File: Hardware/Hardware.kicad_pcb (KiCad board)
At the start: 2 copper layers, 15 parts, among them J1 Conn_01x02, J2 Conn_01x04, J3 Conn_01x03, J4 Conn_01x02, J5 Conn_01x06, J6 Conn_01x08, U1 ESP32-WROOM-32

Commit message: Routing was done
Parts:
- C1, C2, C3: footprint Connector_PinHeader_2.54mm:PinHeader_1x02_P2.54mm_Vertical -> Capacitor_THT:CP_Radial_D4.0mm_P2.00mm
- R1, R2, R3, R4, R5: footprint Connector_PinHeader_2.54mm:PinHeader_1x02_P2.54mm_Vertical -> Resistor_THT:R_Axial_DIN0204_L3.6mm_D1.6mm_P2.54mm_Vertical
- moved J2 85.6 mm to (85.1, 121.9), turned to 90 degrees
- moved J4 68.5 mm to (85.1, 88.9), turned to 180 degrees
- moved R3 62.8 mm to (93.5, 114.3)
- moved R2 59.1 mm to (93.5, 111.8)
- moved R1 49.9 mm to (139.7, 90.2), turned to 90 degrees
- moved R4 49.1 mm to (107.2, 121.4), turned to 90 degrees
- moved C1 33.0 mm to (136.1, 84.3), turned to 180 degrees
- moved R5 32.2 mm to (115.8, 121.4), turned to 90 degrees
- moved C3 27.3 mm to (136.1, 92.9), turned to 180 degrees
- moved C2 26.9 mm to (136.1, 101.6), turned to 180 degrees
- moved J3 26.2 mm to (134.6, 111.8)
- moved J1 12.4 mm to (134.6, 124.5)
- moved J6 11.4 mm to (85.1, 114.3)
- moved J5 4.26 mm to (115.6, 129.5)
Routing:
- net Net-(C1-Pad1): track 0.00 -> 50.2 mm, vias 0 -> 2
- net /IO23: track 0.00 -> 47.5 mm, vias 0 -> 2
- net GND: track 0.00 -> 37.1 mm, vias 0 -> 3
- net /SDI: track 0.00 -> 34.2 mm, vias 0 -> 2
- net Net-(J2-Pad4): track 0.00 -> 25.6 mm, vias 0 -> 3
- net /SDO: track 0.00 -> 24.2 mm, vias 0 -> 1
- net /IO35: track 0.00 -> 21.2 mm
- net /IO33: track 0.00 -> 20.5 mm
- net Net-(J2-Pad3): track 0.00 -> 20.4 mm
- net /RXD: track 0.00 -> 20.3 mm
- net /IO27: track 0.00 -> 19.6 mm
- net /IO25: track 0.00 -> 19.6 mm, vias 0 -> 2
- net /TXD: track 0.00 -> 19.2 mm
- net /Boot_Option: track 0.00 -> 19.2 mm
- net /IO34: track 0.00 -> 19.0 mm, vias 0 -> 2
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- added copper zone on B.Cu, net /VDD33
- added copper zone on B.Cu, net GND

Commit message: quality of life improvements
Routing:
- added copper zone on F.Cu, net /VDD33
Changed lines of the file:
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@@
+    )
+  )
+  (zone (net 3) (net_name /VDD33) (layer B.Cu) (hatch edge 0.508)
+    (connect_pads (clearance 0.508))
+    (min_thickness 0.254)
+    (fill yes (arc_segments 32) (thermal_gap 0.508) (thermal_bridge_width 0.508))
+    (polygon
+      (pts
+        (xy 77.47 78.74) (xy 68.58 80.01) (xy 72.39 68.58)
+      )
+    )
+  )
+  (zone (net 3) (net_name /VDD33) (layer F.Cu) (hatch edge 0.508)
+    (connect_pads (clearance 0.508))
+    (min_thickness 0.254)
+    (fill yes (arc_segments 32) (thermal_gap 0.508) (thermal_bridge_width 0.508))
+    (polygon
+      (pts
+        (xy 95.25 97.79) (xy 127 97.79) (xy 127 78.74) (xy 143.51 78.74) (xy 143.51 135.89)
+        (xy 77.47 135.89) (xy 77.47 78.74) (xy 95.25 78.74)
+      )
     )
   )

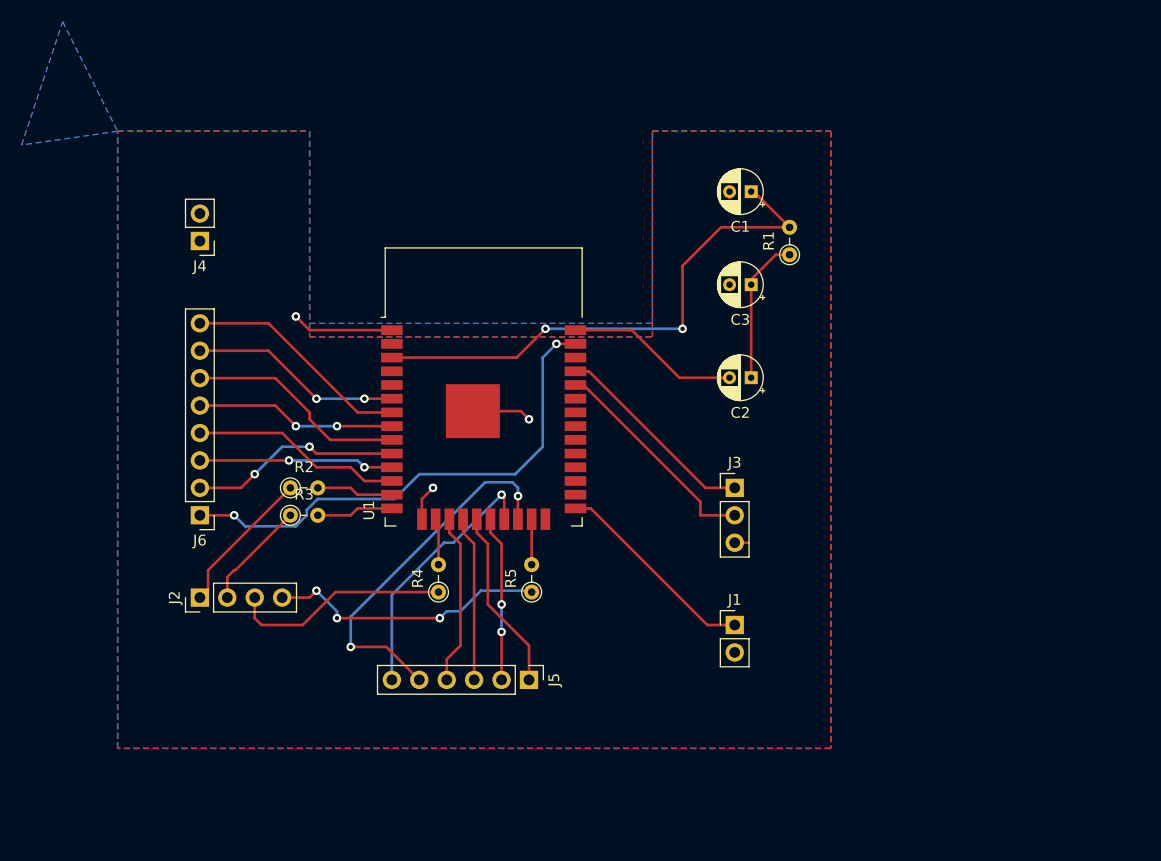
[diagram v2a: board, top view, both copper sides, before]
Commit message: Motor port addition and ground plane fix
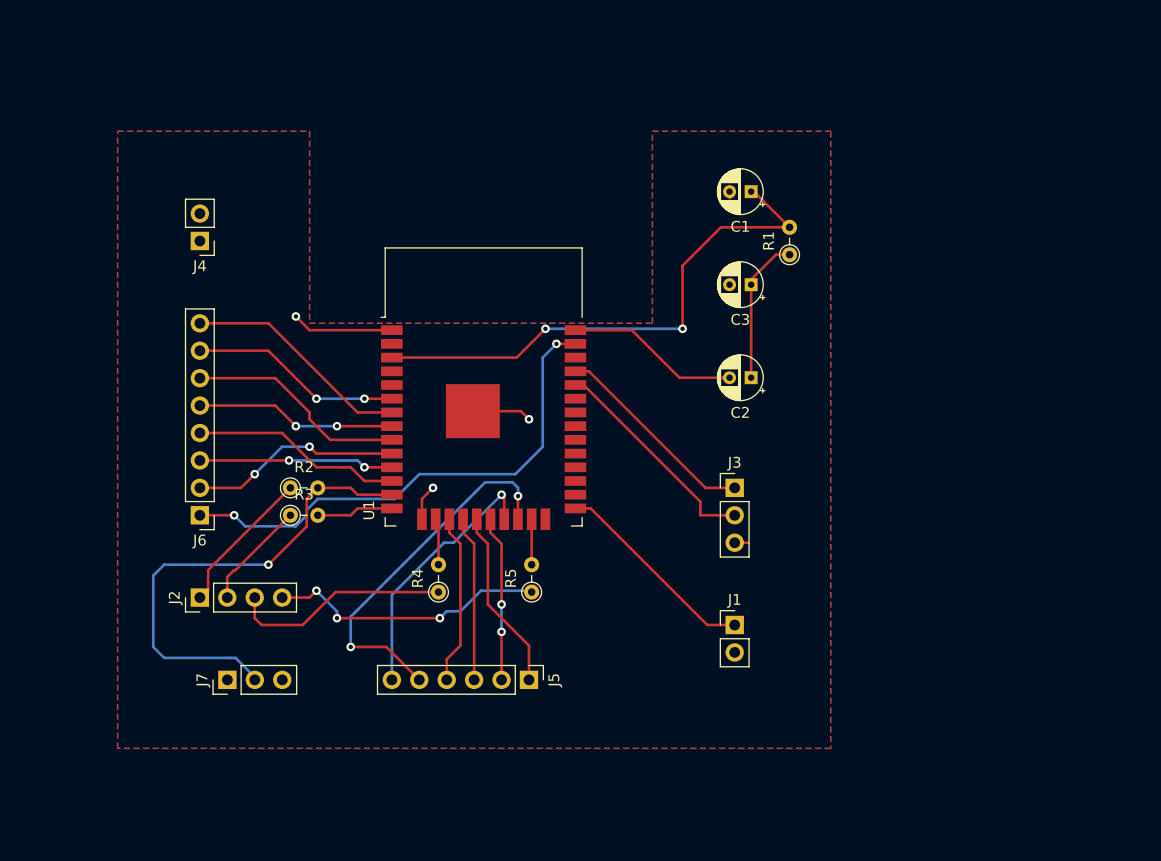
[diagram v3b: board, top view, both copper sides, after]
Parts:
- added J7: Conn_01x03, Connector_PinHeader_2.54mm:PinHeader_1x03_P2.54mm_Vertical, F.Cu at (87.6, 129.5)
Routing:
- net /MTMS: track 7.25 -> 44.9 mm, vias 0 -> 1
- removed copper zone on B.Cu, net /VDD33

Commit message: Silkscreen was added.
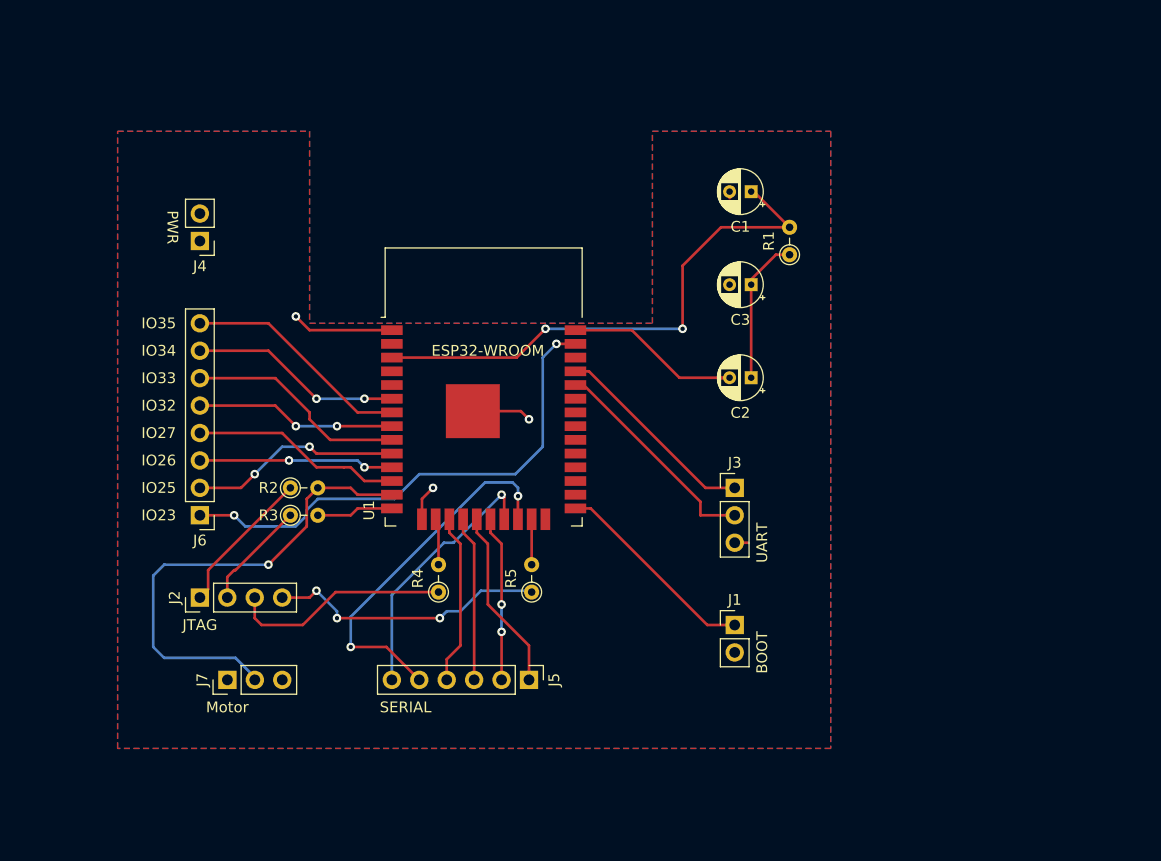
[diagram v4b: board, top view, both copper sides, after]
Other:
- board text added: "BOOT"
- board text added: "ESP32-WROOM"
- board text added: "IO23"
- board text added: "IO25"
- board text added: "IO26"
- board text added: "IO27"
- board text added: "IO32"
- board text added: "IO33"
- board text added: "IO34"
- board text added: "IO35"
- board text added: "JTAG"
- board text added: "Motor"
- board text added: "PWR"
- board text added: "SERIAL"
- board text added: "UART"
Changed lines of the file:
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@@
   (general
     (thickness 1.6)
-    (drawings 4)
+    (drawings 19)
     (tracks 180)
     (zones 0)
@@
   (page A4)
   (layers
-    (0 F.Cu signal)
-    (31 B.Cu signal)
+    (0 F.Cu signal hide)
+    (31 B.Cu signal hide)
     (32 B.Adhes user)
     (33 F.Adhes user)
@@
     (descr "Resistor, Axial_DIN0204 series, Axial, Vertical, pin pitch=2.54mm, 0.167W, length*diameter=3.6*1.6mm^2, http://cdn-reichelt.de/documents/datenblatt/B400/1_4W%23YAG.pdf")
     (tags "Resistor Axial_DIN0204 series Axial Vertical pin pitch 2.54mm 0.167W length 3.6mm diameter 1.6mm")
-    (fp_text reference R3 (at 1.27 -1.92) (layer F.SilkS)
+    (fp_text reference R3 (at -2.032 0) (layer F.SilkS)
       (effects (font (size 1 1) (thickness 0.15)))
     )
@@
     (descr "Resistor, Axial_DIN0204 series, Axial, Vertical, pin pitch=2.54mm, 0.167W, length*diameter=3.6*1.6mm^2, http://cdn-reichelt.de/documents/datenblatt/B400/1_4W%23YAG.pdf")
     (tags "Resistor Axial_DIN0204 series Axial Vertical pin pitch 2.54mm 0.167W length 3.6mm diameter 1.6mm")
-    (fp_text reference R2 (at 1.27 -1.92) (layer F.SilkS)
+    (fp_text reference R2 (at -2.032 0) (layer F.SilkS)
       (effects (font (size 1 1) (thickness 0.15)))
     )
@@
     )
   )
+  (gr_text SERIAL (at 104.14 132.08) (layer F.SilkS)
+    (effects (font (size 1 1) (thickness 0.15)))
+  )
+  (gr_text BOOT (at 137.16 127 90) (layer F.SilkS)
+    (effects (font (size 1 1) (thickness 0.15)))
+  )
+  (gr_text UART (at 137.16 116.84 90) (layer F.SilkS)
+    (effects (font (size 1 1) (thickness 0.15)))
+  )
+  (gr_text ESP32-WROOM (at 111.76 99.06) (layer F.SilkS)
+    (effects (font (size 1 1) (thickness 0.15)))
+  )
+  (gr_text PWR (at 82.55 87.63 270) (layer F.SilkS)
+    (effects (font (size 1 1) (thickness 0.15)))
+  )
+  (gr_text IO35 (at 81.28 96.52) (layer F.SilkS)
+    (effects (font (size 1 1) (thickness 0.15)))
+  )
+  (gr_text IO34 (at 81.28 99.06) (layer F.SilkS)
+    (effects (font (size 1 1) (thickness 0.15)))
+  )
+  (gr_text IO33 (at 81.28 101.6) (layer F.SilkS)
+    (effects (font (size 1 1) (thickness 0.15)))
+  )
+  (gr_text IO32 (at 81.28 104.14) (layer F.SilkS)
+    (effects (font (size 1 1) (thickness 0.15)))
+  )
+  (gr_text IO27 (at 81.28 106.68) (layer F.SilkS)
+    (effects (font (size 1 1) (thickness 0.15)))
+  )
+  (gr_text IO26 (at 81.28 109.22) (layer F.SilkS)
+    (effects (font (size 1 1) (thickness 0.15)))
+  )
+  (gr_text IO25 (at 81.28 111.76) (layer F.SilkS)
+    (effects (font (size 1 1) (thickness 0.15)))
+  )
+  (gr_text IO23 (at 81.28 114.3) (layer F.SilkS)
+    (effects (font (size 1 1) (thickness 0.15)))
+  )
+  (gr_text JTAG (at 85.09 124.46) (layer F.SilkS)
+    (effects (font (size 1 1) (thickness 0.15)))
+  )
+  (gr_text Motor (at 87.63 132.08) (layer F.SilkS)
+    (effects (font (size 1 1) (thickness 0.15)))
+  )
   (gr_line (start 143.51 78.74) (end 77.47 78.74) (layer Dwgs.User) (width 0.15))

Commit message: battery connector update
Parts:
- J4: footprint Connector_PinHeader_2.54mm:PinHeader_1x02_P2.54mm_Vertical -> Connector_PinHeader_1.00mm:PinHeader_1x02_P1.00mm_Vertical
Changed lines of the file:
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@@
     (add_net "Net-(U1-Pad5)")
+  )
+  (module Connector_PinHeader_1.00mm:PinHeader_1x02_P1.00mm_Vertical (layer F.Cu)
+    (at 85.09 88.9 180)
+    (descr "Through hole straight pin header, 1x02, 1.00mm pitch, single row")
+    (tags "Through hole pin header THT 1x02 1.00mm single row")
+    (fp_text reference J4 (at 0 -1.56) (layer F.SilkS)
+      (effects (font (size 1 1) (thickness 0.15)))
+    )
+    (fp_text value Conn_01x02 (at 0 2.56) (layer F.Fab)
+      (effects (font (size 1 1) (thickness 0.15)))
+    )
+    (fp_text user %R (at 0 0.5 90) (layer F.Fab)
+      (effects (font (size 0.76 0.76) (thickness 0.114)))
+    )
+    (fp_line (start -0.3175 -0.5) (end 0.635 -0.5) (layer F.Fab) (width 0.1))
+    (fp_line (start 0.635 -0.5) (end 0.635 1.5) (layer F.Fab) (width 0.1))
+    (fp_line (start 0.635 1.5) (end -0.635 1.5) (layer F.Fab) (width 0.1))
+    (fp_line (start -0.635 1.5) (end -0.635 -0.1825) (layer F.Fab) (width 0.1))
+    (fp_line (start -0.635 -0.1825) (end -0.3175 -0.5) (layer F.Fab) (width 0.1))
+    (fp_line (start -0.695 1.56) (end -0.394493 1.56) (layer F.SilkS) (width 0.12))
+    (fp_line (start 0.394493 1.56) (end 0.695 1.56) (layer F.SilkS) (width 0.12))
+    (fp_line (start -0.695 0.685) (end -0.695 1.56) (layer F.SilkS) (width 0.12))
+    (fp_line (start 0.695 0.685) (end 0.695 1.56) (layer F.SilkS) (width 0.12))
+    (fp_line (start -0.695 0.685) (end -0.608276 0.685) (layer F.SilkS) (width 0.12))
+    (fp_line (start 0.608276 0.685) (end 0.695 0.685) (layer F.SilkS) (width 0.12))
+    (fp_line (start -0.695 0) (end -0.695 -0.685) (layer F.SilkS) (width 0.12))
+    (fp_line (start -0.695 -0.685) (end 0 -0.685) (layer F.SilkS) (width 0.12))
+    (fp_line (start -1.15 -1) (end -1.15 2) (layer F.CrtYd) (width 0.05))
+    (fp_line (start -1.15 2) (end 1.15 2) (layer F.CrtYd) (width 0.05))
+    (fp_line (start 1.15 2) (end 1.15 -1) (layer F.CrtYd) (width 0.05))
+    (fp_line (start 1.15 -1) (end -1.15 -1) (layer F.CrtYd) (width 0.05))
+    (pad 2 thru_hole oval (at 0 1 180) (size 0.85 0.85) (drill 0.5) (layers *.Cu *.Mask)
+      (net 1 GND))
+    (pad 1 thru_hole rect (at 0 0 180) (size 0.85 0.85) (drill 0.5) (layers *.Cu *.Mask)
+      (net 3 /VDD33))
+    (model ${KISYS3DMOD}/Connector_PinHeader_1.00mm.3dshapes/PinHeader_1x02_P1.00mm_Vertical.wrl
+      (at (xyz 0 0 0))
+      (scale (xyz 1 1 1))
+      (rotate (xyz 0 0 0))
+    )
   )
   (module Connector_PinHeader_2.54mm:PinHeader_1x03_P2.54mm_Vertical (layer F.Cu)
@@
     )
   )
-  (module Connector_PinHeader_2.54mm:PinHeader_1x02_P2.54mm_Vertical (layer F.Cu)
-    (at 85.09 88.9 180)
-    (descr "Through hole straight pin header, 1x02, 2.54mm pitch, single row")
-    (tags "Through hole pin header THT 1x02 2.54mm single row")
-    (fp_text reference J4 (at 0 -2.33) (layer F.SilkS)
-      (effects (font (size 1 1) (thickness 0.15)))
-    )
-    (fp_text value Conn_01x02 (at 0 4.87) (layer F.Fab)
-      (effects (font (size 1 1) (thickness 0.15)))
-    )
-    (fp_line (start -0.635 -1.27) (end 1.27 -1.27) (layer F.Fab) (width 0.1))
-    (fp_line (start 1.27 -1.27) (end 1.27 3.81) (layer F.Fab) (width 0.1))
-    (fp_line (start 1.27 3.81) (end -1.27 3.81) (layer F.Fab) (width 0.1))
-    (fp_line (start -1.27 3.81) (end -1.27 -0.635) (layer F.Fab) (width 0.1))
-    (fp_line (start -1.27 -0.635) (end -0.635 -1.27) (layer F.Fab) (width 0.1))
-    (fp_line (start -1.33 3.87) (end 1.33 3.87) (layer F.SilkS) (width 0.12))
-    (fp_line (start -1.33 1.27) (end -1.33 3.87) (layer F.SilkS) (width 0.12))
-    (fp_line (start 1.33 1.27) (end 1.33 3.87) (layer F.SilkS) (width 0.12))
-    (fp_line (start -1.33 1.27) (end 1.33 1.27) (layer F.SilkS) (width 0.12))
-    (fp_line (start -1.33 0) (end -1.33 -1.33) (layer F.SilkS) (width 0.12))
-    (fp_line (start -1.33 -1.33) (end 0 -1.33) (layer F.SilkS) (width 0.12))
-    (fp_line (start -1.8 -1.8) (end -1.8 4.35) (layer F.CrtYd) (width 0.05))
-    (fp_line (start -1.8 4.35) (end 1.8 4.35) (layer F.CrtYd) (width 0.05))
-    (fp_line (start 1.8 4.35) (end 1.8 -1.8) (layer F.CrtYd) (width 0.05))
-    (fp_line (start 1.8 -1.8) (end -1.8 -1.8) (layer F.CrtYd) (width 0.05))
-    (fp_text user %R (at 0 1.27 90) (layer F.Fab)
-      (effects (font (size 1 1) (thickness 0.15)))
-    )
-    (pad 2 thru_hole oval (at 0 2.54 180) (size 1.7 1.7) (drill 1) (layers *.Cu *.Mask)
-      (net 1 GND))
-    (pad 1 thru_hole rect (at 0 0 180) (size 1.7 1.7) (drill 1) (layers *.Cu *.Mask)
-      (net 3 /VDD33))
-    (model ${KISYS3DMOD}/Connector_PinHeader_2.54mm.3dshapes/PinHeader_1x02_P2.54mm_Vertical.wrl
-      (at (xyz 0 0 0))
-      (scale (xyz 1 1 1))
-      (rotate (xyz 0 0 0))
-    )
-  )
   (module Connector_PinHeader_2.54mm:PinHeader_1x06_P2.54mm_Vertical locked (layer F.Cu)
     (at 115.57 129.54 270)
@@
     (effects (font (size 1 1) (thickness 0.15)))
   )
-  (gr_text PWR (at 82.55 87.63 270) (layer F.SilkS)
+  (gr_text PWR (at 83.058 88.392 270) (layer F.SilkS)
     (effects (font (size 1 1) (thickness 0.15)))
   )
